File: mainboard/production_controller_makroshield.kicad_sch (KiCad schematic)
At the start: 66 parts, among them J1 CON_TERM_BLK_1X2_TB008A-508-0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, J2 CON_TERM_BLK_1X2_TB008A-508-0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, J3 CON_HDR_MIKROBUS_ADDON_TH, J4 CON_TERM_BLK_1X2_TB008A-508-0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, J5 CON_HDR_MIKROBUS_SOCKET_TH, J6 CON_HDR_100MILS_M_TH_1X3, Q1 TRX_PMOS_AOD4189, Q2 TRX_2NPN_BC846S,115, U1 IO_EXP_PI4IOE5V6416ZDEX, U2 IO_EXP_PI4IOE5V6416ZDEX, U3 SEN_TEMP_TMP1075DR, U4 SEN_CUR_ACS711KEXLT-31AB-T, U5 ADC_NAU7802SGI

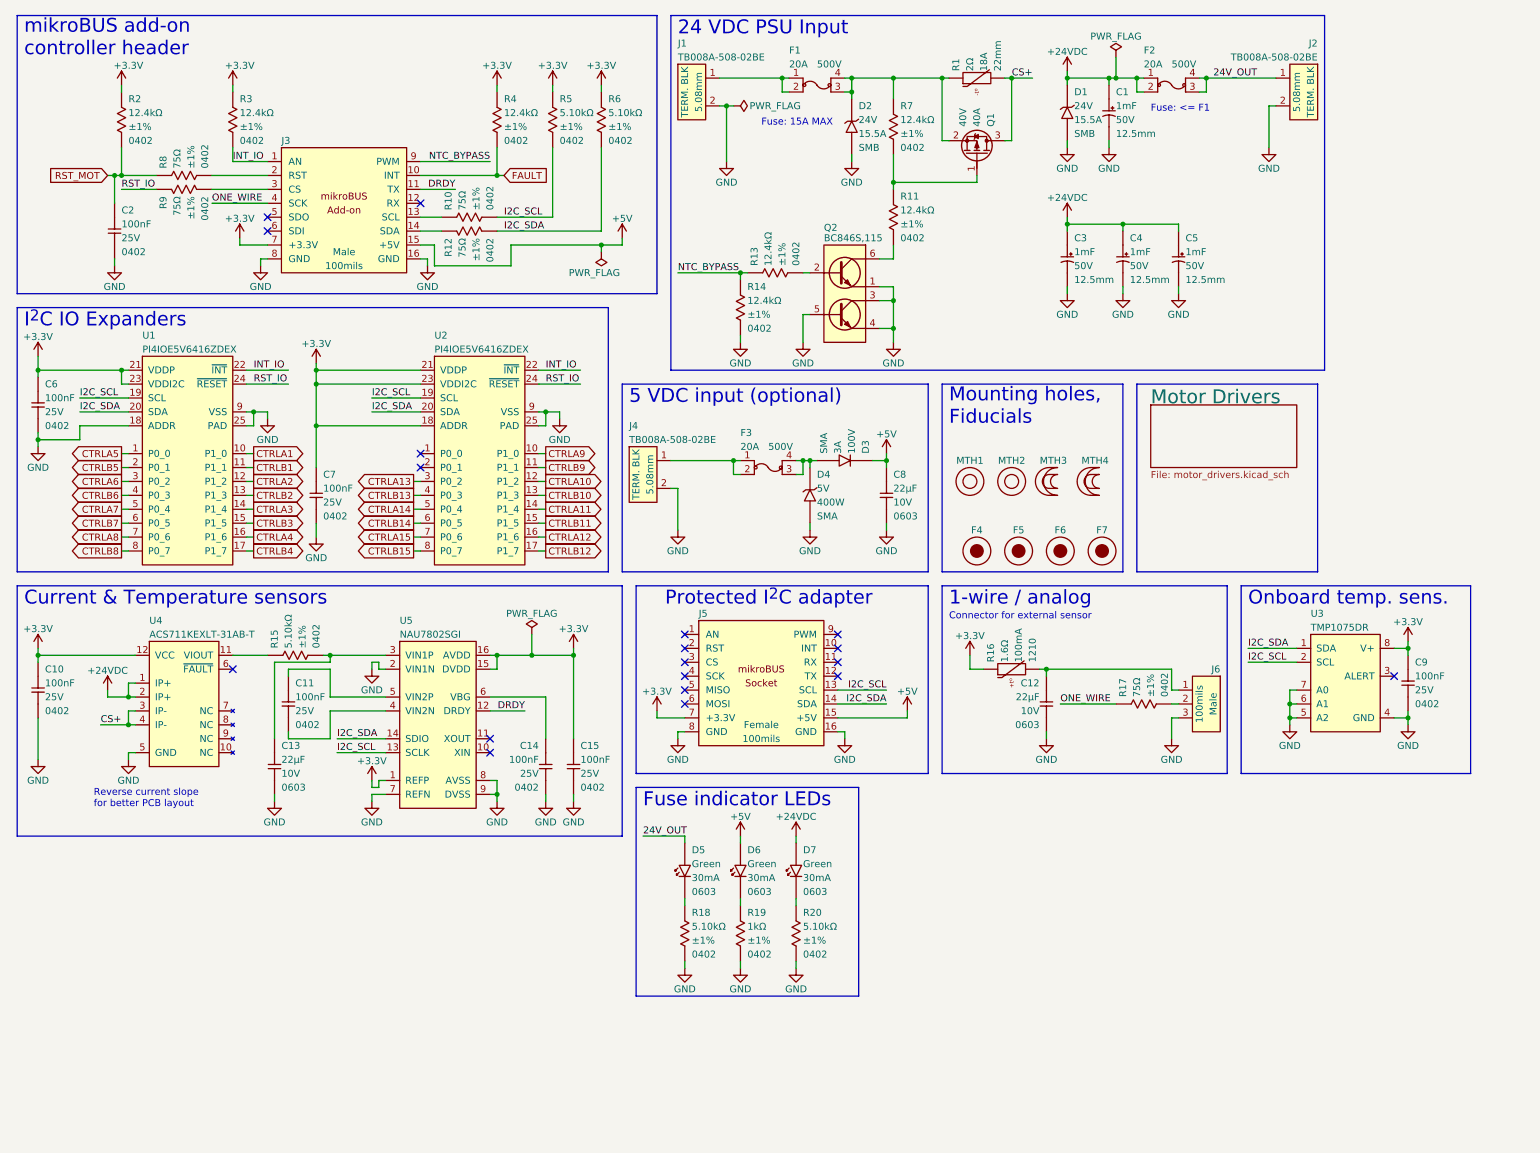
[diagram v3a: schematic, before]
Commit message: Add 4 extra IOs (SVG connectors)
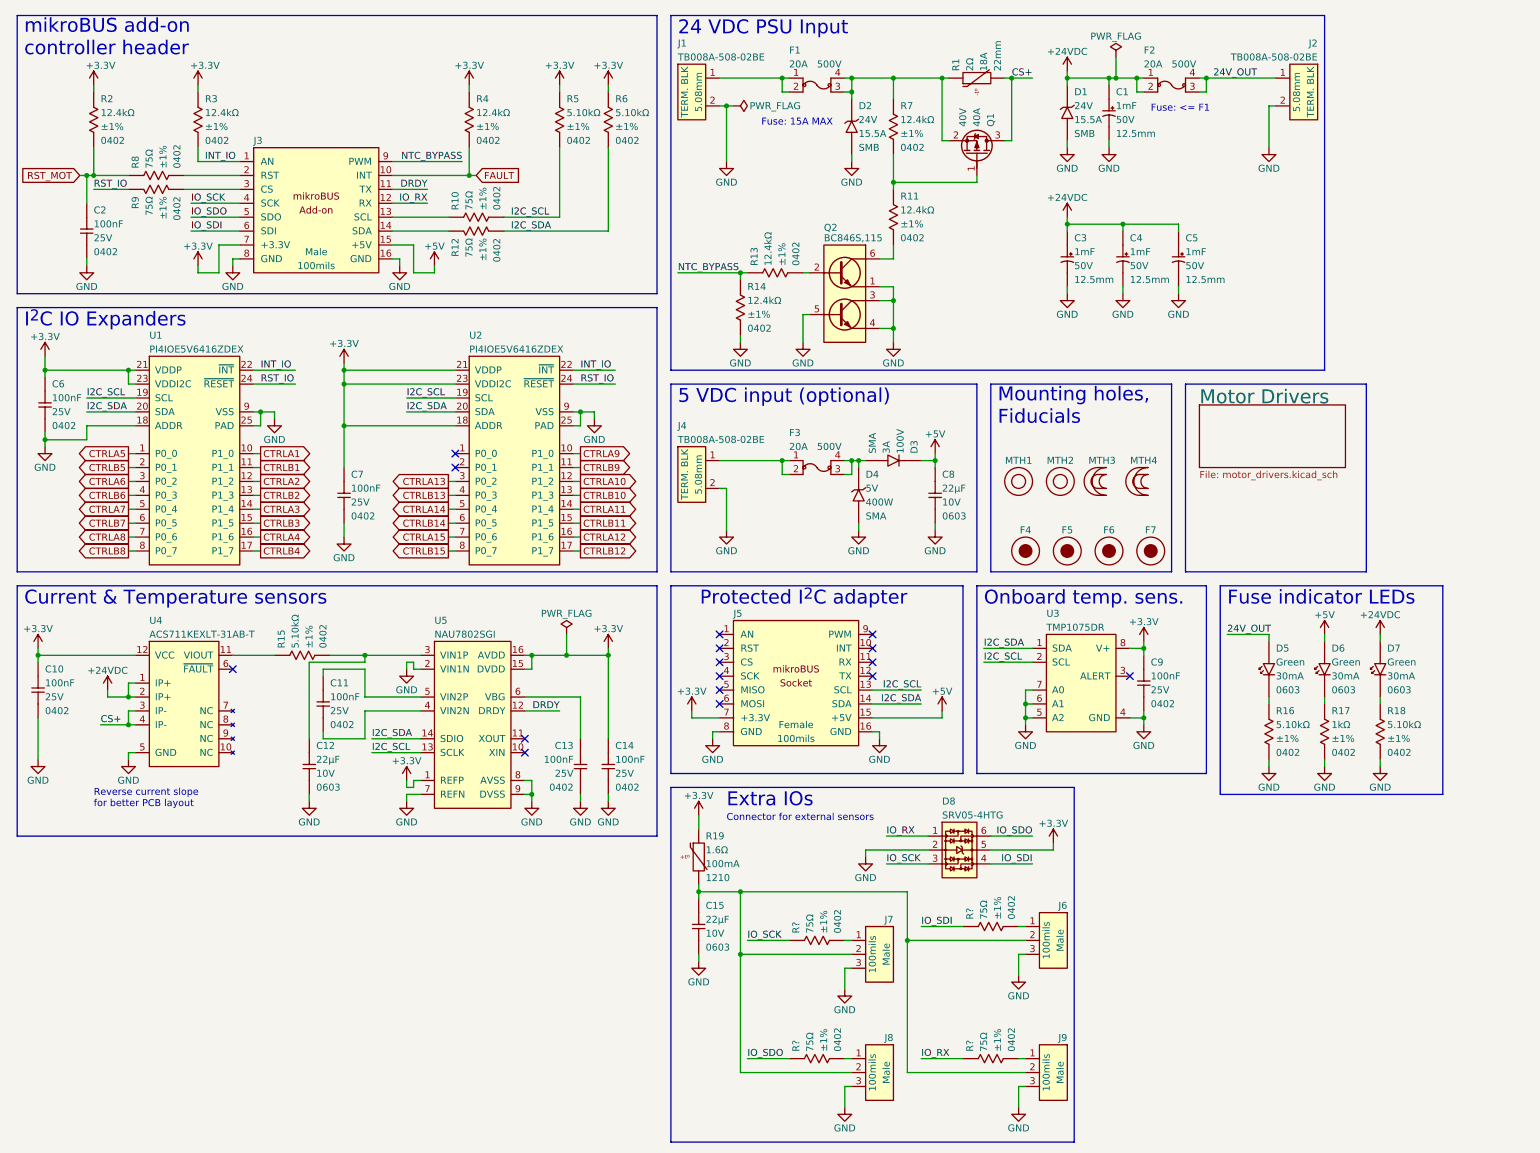
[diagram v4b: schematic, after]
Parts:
- removed R16: PTC_SMD1210B010TF, connaxio-resistors:RES_1210_3225M, symbol connaxio-resistors:PTC_SMD1210B010TF
- removed R17: RES_226Ω_1%_0402, connaxio-resistors:RES_0402_1005M, symbol connaxio-resistors:RES_75Ω_1%_0402
- added D8: DIO_TVS_SRV05-4HTG, connaxio-sop:SOT-23-6, symbol connaxio-diodes:DIO_TVS_SRV05-4HTG
- added J6, J8, J9: CON_HDR_100MILS_M_TH_1X3, connaxio-connectors:CON_HDR_100MILS_M_TH_1X3, symbol connaxio-connectors:CON_HDR_100MILS_M_TH_1X3
- added R19: PTC_SMD1210B010TF, connaxio-resistors:RES_1210_3225M, symbol connaxio-resistors:PTC_SMD1210B010TF
- added R? (x4): RES_226Ω_1%_0402, connaxio-resistors:RES_0402_1005M, symbol connaxio-resistors:RES_75Ω_1%_0402
- MTH1, MTH2, MTH3, MTH4: Property 5.5mm -> M5
- renumbered C13 to C12, C14 to C13, C15 to C14, C12 to C15, J6 to J7, R18 to R16, R19 to R17, R20 to R18
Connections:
- net +3.3V: now also D8.5, R19.1
- net GND: now also D8.2, J6.3, J8.3, J9.3
- net at J7.1: now also R?.2; no longer C15.1
- net at J7.2: now also C15.1, J6.2, J8.2, J9.2, R19.2
- net IO_RX: now reaches J3.12 (RX)
- net IO_RX: now also D8.1, R?.1
- net IO_SDO: now reaches J3.5 (SDO)
- net IO_SDO: now also D8.6, R?.1
- net IO_SDI: now reaches J3.6 (SDI)
- net IO_SDI: now also D8.4, R?.1
- net ONE_WIRE renamed IO_SCK
- net IO_SCK: now also D8.3, R?.1
- new net: J9.1, R?.2
- new net: J8.1, R?.2
- new net: J6.1, R?.2
- no-connect marks 19 -> 16
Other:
- note added: "Connector for external sensors"
- note added: "Extra IOs"
- note removed: "1-wire / analog"
- note removed: "Connector for external sensor"
- moved on the sheet: C11, C12, C13, C14, C15, C2, C6, C7, C8, C9, D3, D4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
